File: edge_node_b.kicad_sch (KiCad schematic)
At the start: 5 parts

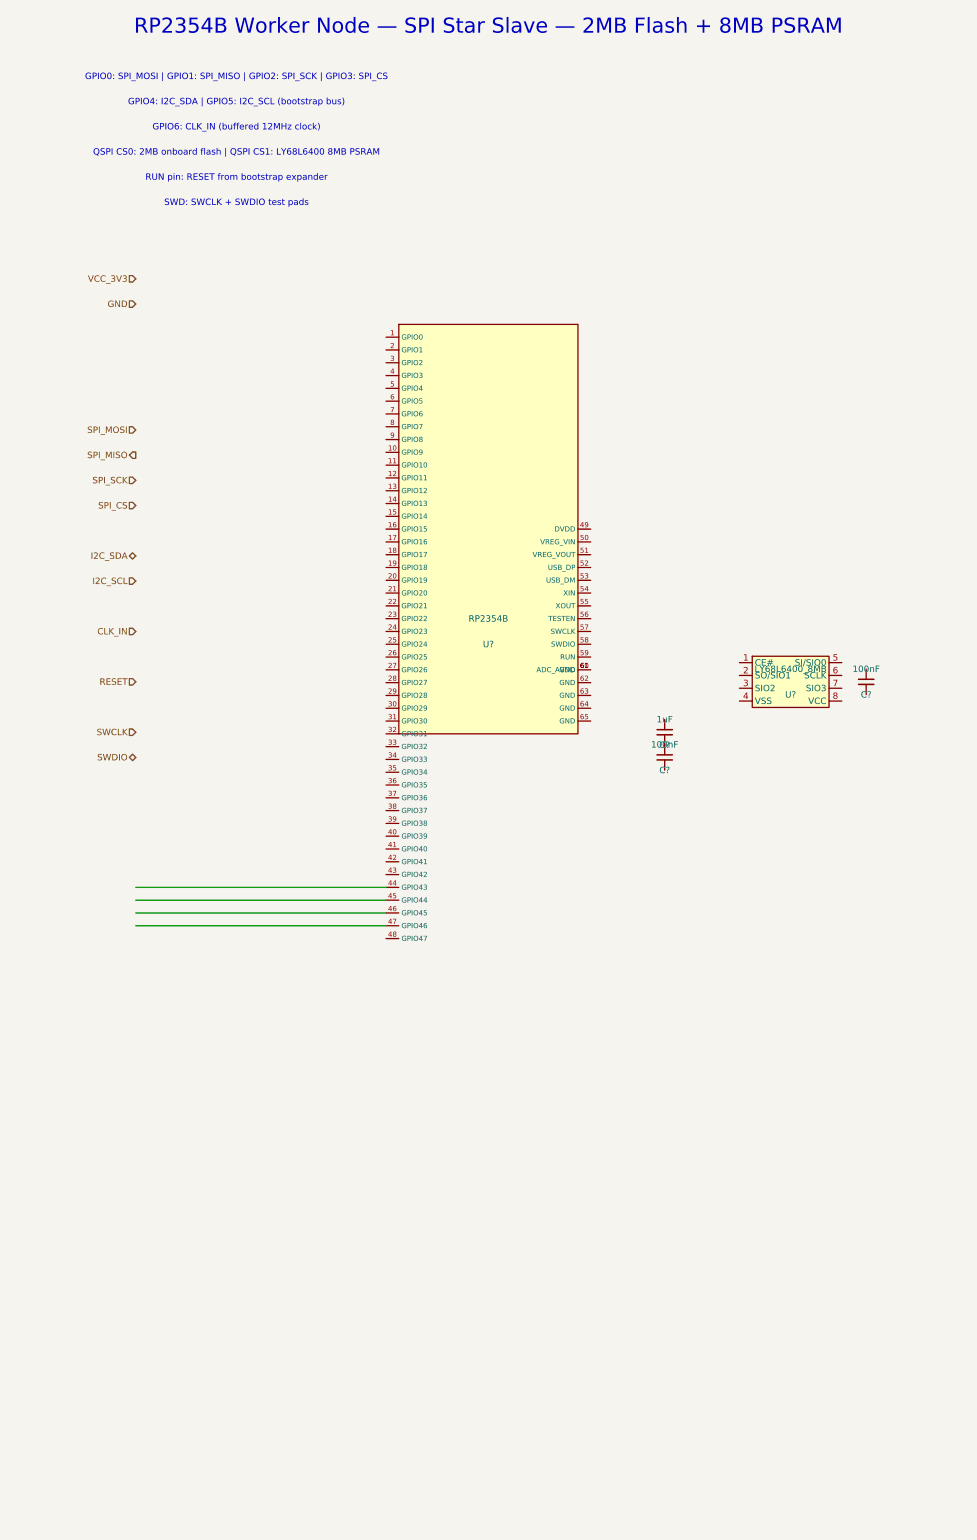
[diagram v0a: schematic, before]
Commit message: Regenerate KiCad output files for v1.0 architecture
Co-authored-by: Copilot <223556219+Copilot@users.noreply.github.com>
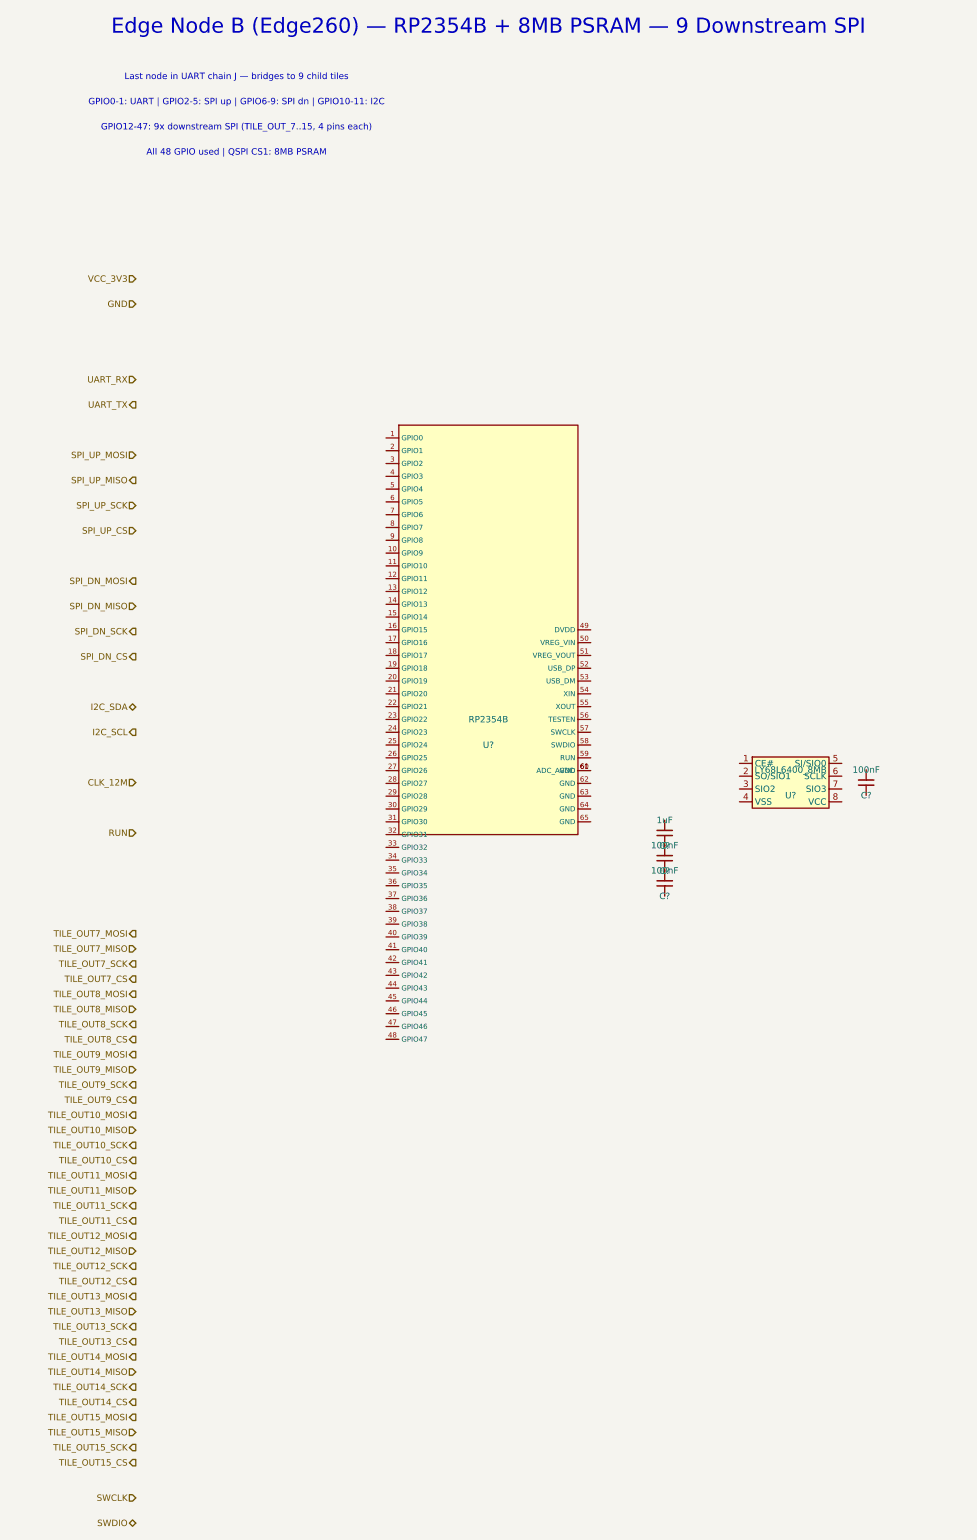
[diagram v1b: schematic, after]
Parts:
- removed C? (x2): 100nF, symbol Device:C
- removed C?: 1uF, symbol Device:C
- removed U?: RP2354B, symbol MCU_RaspberryPi:RP2354B
- removed U?: LY68L6400_8MB, symbol Memory_RAM:LY68L6400
- added C? (x3): 100nF, symbol Device:C
- added C?: 1uF, symbol Device:C
- added U?: RP2354B, symbol MCU_RaspberryPi:RP2354B
- added U?: LY68L6400_8MB, symbol Memory_RAM:LY68L6400
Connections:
- new net: U?.60 (ADC_AVDD), U?.61 (GND)
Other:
- note added: "All 48 GPIO used | QSPI CS1: 8MB PSRAM"
- note added: "Edge Node B (Edge260) — RP2354B + 8MB PSRAM — 9 Downstream SPI"
- note added: "GPIO0-1: UART | GPIO2-5: SPI up | GPIO6-9: SPI dn | GPIO10-11: I2C"
- note added: "GPIO12-47: 9x downstream SPI (TILE_OUT_7..15, 4 pins each)"
- note added: "Last node in UART chain J — bridges to 9 child tiles"
- note removed: "GPIO0: SPI_MOSI | GPIO1: SPI_MISO | GPIO2: SPI_SCK | GPIO3: SPI_CS"
- note removed: "GPIO4: I2C_SDA | GPIO5: I2C_SCL (bootstrap bus)"
- note removed: "GPIO6: CLK_IN (buffered 12MHz clock)"
- note removed: "QSPI CS0: 2MB onboard flash | QSPI CS1: LY68L6400 8MB PSRAM"
- note removed: "RP2354B Worker Node — SPI Star Slave — 2MB Flash + 8MB PSRAM"
- note removed: "RUN pin: RESET from bootstrap expander"
- note removed: "SWD: SWCLK + SWDIO test pads"
- title: Worker Node (RP2354B + 8MB PSRAM) — SPI Star Slave -> Edge Node B (Edge260) — 9 Downstream SPI + PSRAM
